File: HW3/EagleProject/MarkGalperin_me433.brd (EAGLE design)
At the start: 100 x 100 mm, 22 parts, among them J1 USB-MB-H

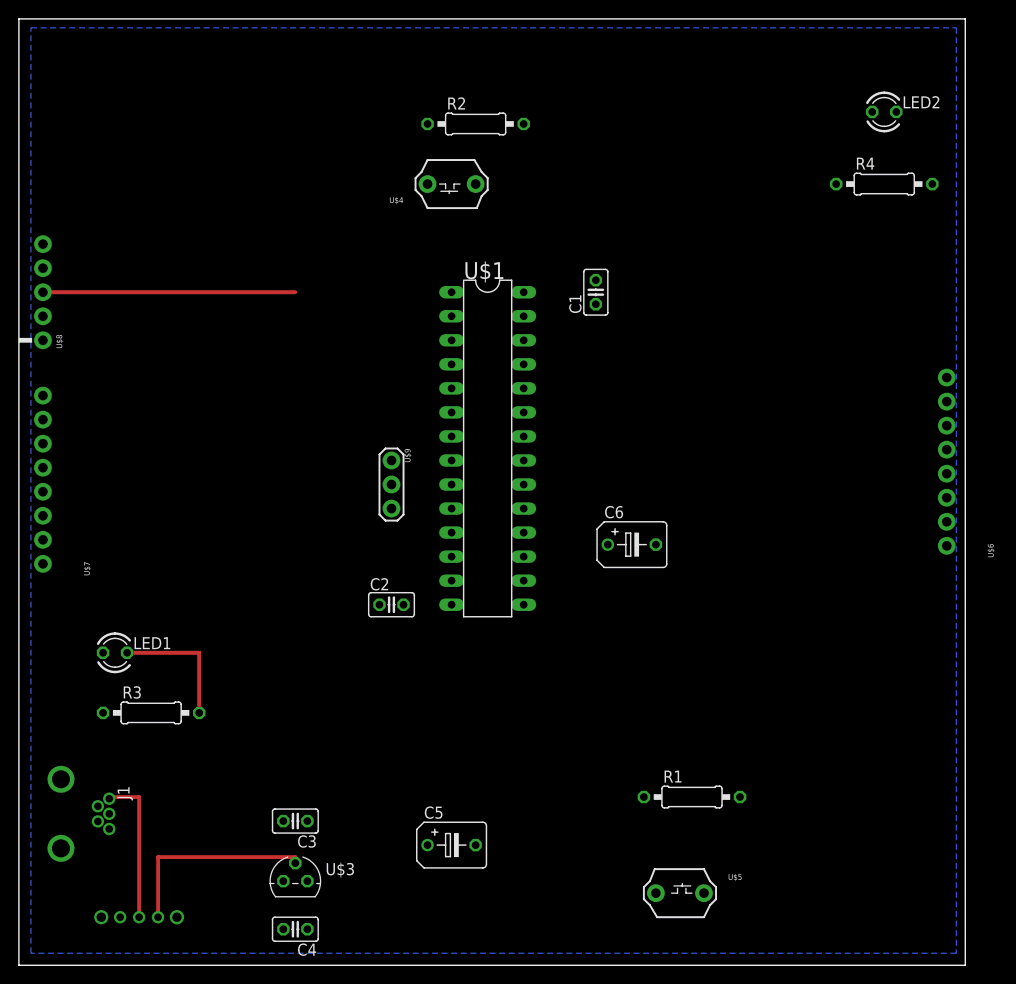
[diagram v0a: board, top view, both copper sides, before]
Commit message: finished the board wiring, checked DRC and ERC. Still have to change the PIC footprint and make Gerber files
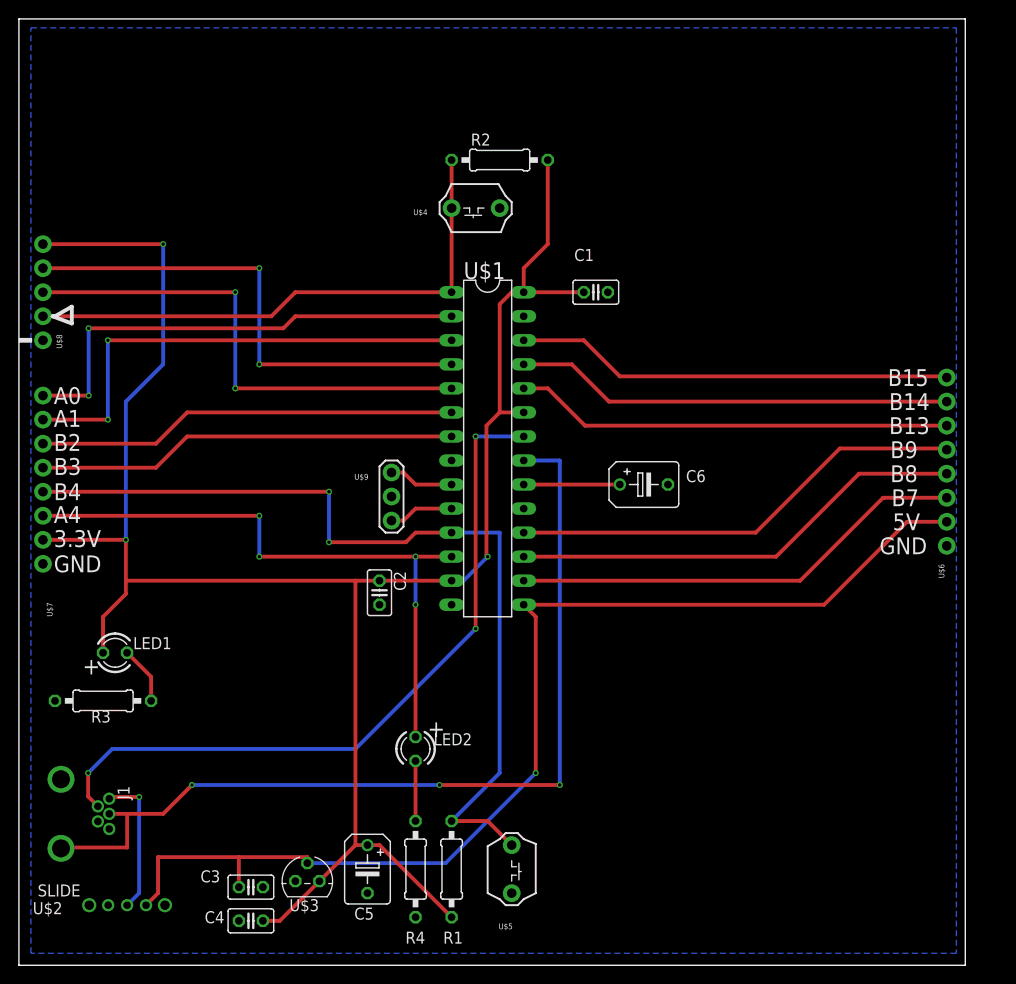
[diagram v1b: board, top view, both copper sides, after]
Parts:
- moved R4 87.7 mm to (41.9, 10.2), turned to 90 degrees
- moved LED2 83.6 mm to (41.9, 22.9), turned to 270 degrees
- moved R1 26.5 mm to (45.7, 10.2), turned to 270 degrees
- moved U$5 21.6 mm to (50.8, 7.62), turned to 270 degrees
- moved C5 9.25 mm to (36.8, 10.2), turned to 270 degrees
- moved C3 8.42 mm to (24.5, 8.26), turned to 0 degrees
- moved C6 6.48 mm to (66.0, 50.8)
- moved R3 5.24 mm to (8.89, 27.9)
- moved C4 4.78 mm to (24.5, 4.70)
- moved R2 4.58 mm to (50.8, 85.1)
- moved U$4 3.59 mm to (45.7, 81.3)
- moved U$2 1.80 mm to (11.4, 6.35)
- moved C2 1.80 mm to (38.1, 39.4), turned to 270 degrees
- moved U$3 1.27 mm to (30.5, 8.89)
- moved U$9 1.27 mm to (36.8, 49.5)
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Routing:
- net +3V3: track 0.00 -> 215.2 mm, vias 0 -> 3
- net +5V: track 21.5 -> 119.9 mm, vias 0 -> 1
- net D+: track 0.00 -> 97.5 mm, vias 0 -> 3
- net B4/USER: track 0.00 -> 94.0 mm, vias 0 -> 2
- net D-: track 0.00 -> 76.6 mm, vias 0 -> 3
- net A4/LED: track 0.00 -> 66.5 mm, vias 0 -> 4
- net MCLR: track 0.00 -> 58.2 mm
- net PGD: track 0.00 -> 53.3 mm, vias 0 -> 2
- net A1: track 0.00 -> 51.6 mm, vias 0 -> 2
- net A0: track 0.00 -> 50.8 mm, vias 0 -> 2
- net B9: track 0.00 -> 48.5 mm
- net B8: track 0.00 -> 48.3 mm
- net B7: track 0.00 -> 48.3 mm
- net B15: track 0.00 -> 46.3 mm
- net B14: track 0.00 -> 46.3 mm
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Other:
- board text added: "+"
- board text added: "3.3V"
- board text added: "5V"
- board text added: "A0"
- board text added: "A1"
- board text added: "A4"
- board text added: "B13"
- board text added: "B14"
- board text added: "B15"
- board text added: "B2"
- board text added: "B3"
- board text added: "B4"
- board text added: "B7"
- board text added: "B8"
- board text added: "B9"
- board text added: "GND"
